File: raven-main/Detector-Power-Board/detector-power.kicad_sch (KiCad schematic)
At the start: 35 parts, among them J1 DeployLipo, J9 UCLipo, Q1 SQJQ100EL, T1 Transformer_1P_1S, U6 LM5185QPWPRQ1, U7 TPS7A4701xRGW, U8 TPS7A4701xRGW

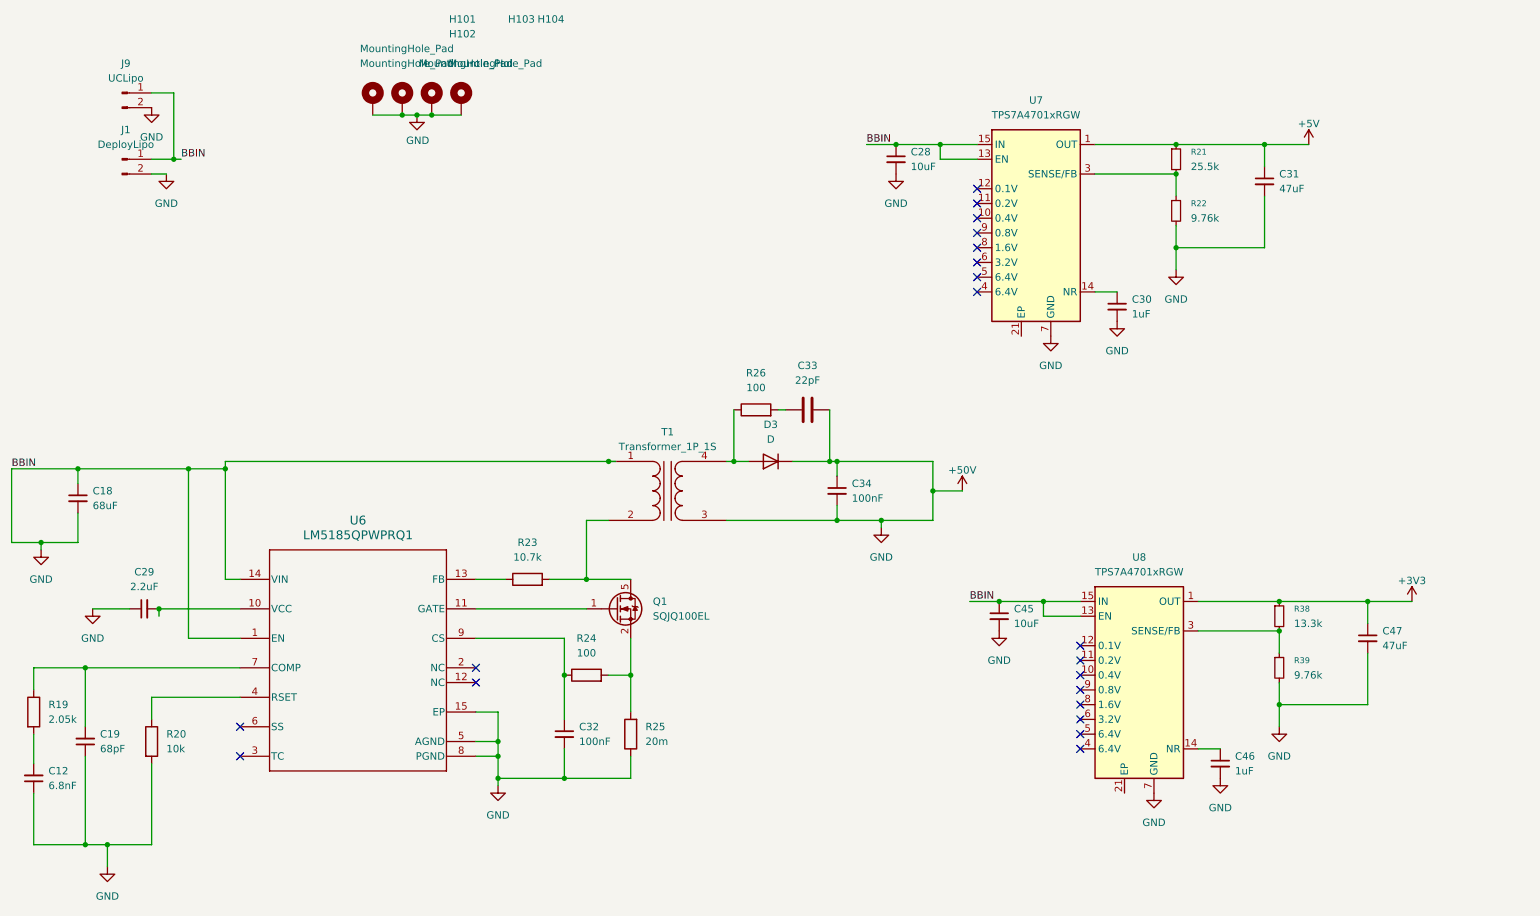
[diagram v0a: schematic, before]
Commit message: Added detector integration to power
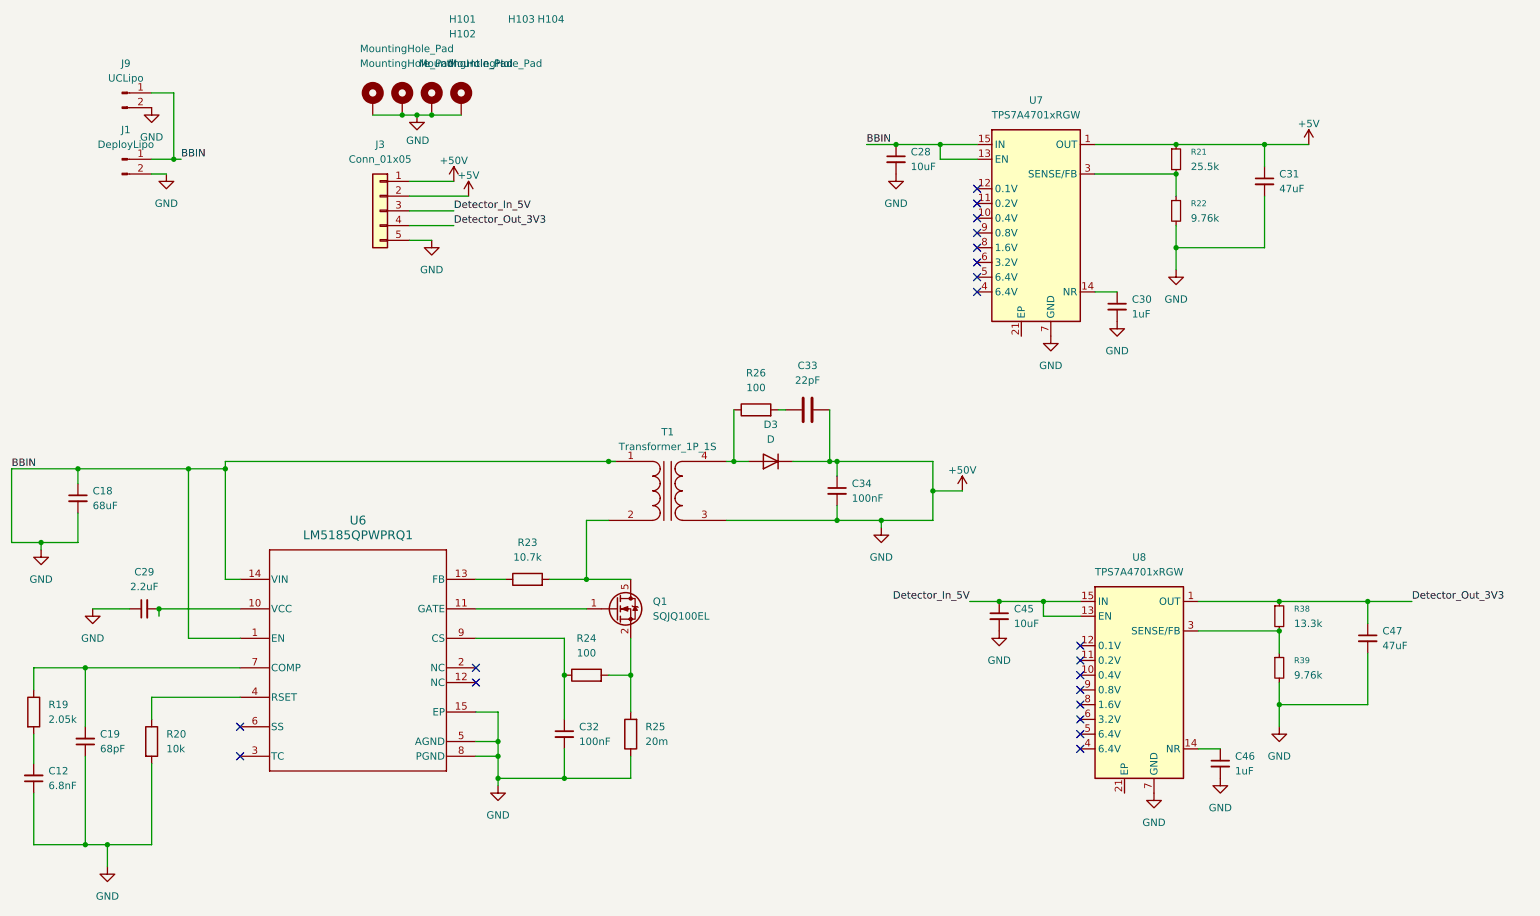
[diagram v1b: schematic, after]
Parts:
- added J3: Conn_01x05, symbol Connector_Generic:Conn_01x05
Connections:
- net +50V: now also J3.1 (Pin_1), J3.5 (Pin_5); no longer C45.1, U8.13 (EN), U8.15 (IN), U8.16 (IN)
- net +5V: now also J3.2 (Pin_2)
- net +3V3 renamed Detector_Out_3V3
- net Detector_Out_3V3: now also J3.4 (Pin_4)
- new net Detector_In_5V: C45.1, J3.3 (Pin_3), U8.13 (EN), U8.15 (IN), U8.16 (IN)

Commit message: Added on/off
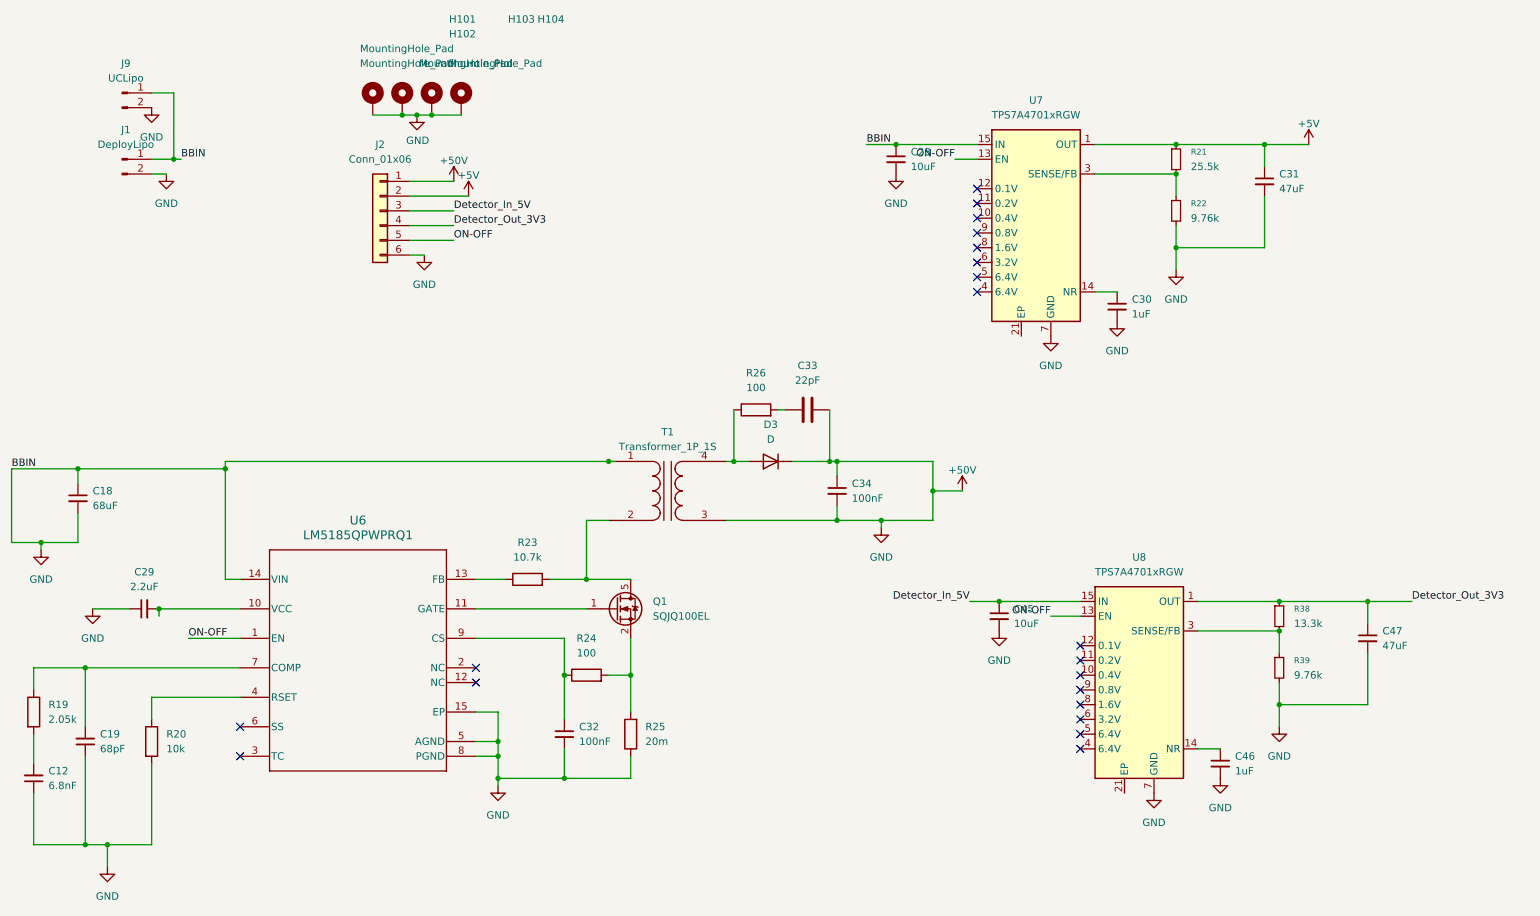
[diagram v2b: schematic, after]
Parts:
- removed J3: Conn_01x05, symbol Connector_Generic:Conn_01x05
- added J2: Conn_01x06, symbol Connector_Generic:Conn_01x06
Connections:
- net +50V: now also J2.1 (Pin_1), J2.6 (Pin_6); no longer U6.1 (EN), U7.13 (EN)
- net +5V: now also J2.2 (Pin_2)
- net Detector_In_5V: now also J2.3 (Pin_3); no longer U8.13 (EN)
- net Detector_Out_3V3: now also J2.4 (Pin_4)
- new net ON-OFF: J2.5 (Pin_5), U6.1 (EN), U7.13 (EN), U8.13 (EN)

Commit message: Organising parts in layout
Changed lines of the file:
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@@
-	)
-	(junction
-		(at 63.5 120.65)
-		(diameter 0)
-		(color 0 0 0 0)
 	)
 	(junction
@@
 		)
 		(stroke
-			(width 0)
-			(type default)
-		)
-	)
-	(wire
-		(pts
-			(xy 63.5 120.65) (xy 63.5 121.92)
-		)
-		(stroke

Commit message: Relabelled power board
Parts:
- J2: footprint (none) -> TerminalBlock_4Ucon:TerminalBlock_4Ucon_1x06_P3.50mm_Horizontal
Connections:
- net +50V renamed GND
- net +5V renamed Power_Out_5V
- net Detector_In_5V renamed Data_In_5V
- net Detector_Out_3V3 renamed Data_Out_3V3

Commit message: Corrected boost
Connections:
- net GND: no longer C18.1, C28.1, C33.2, C34.1, D3.1 (K), J1.1 (Pin_1), J2.1 (Pin_1), J9.1 (Pin_1), T1.1 (AA), U6.14 (VIN), U7.15 (IN), U7.16 (IN)
- new net BBIN: C18.1, C28.1, J1.1 (Pin_1), J9.1 (Pin_1), T1.1 (AA), U6.14 (VIN), U7.15 (IN), U7.16 (IN)
- new net Power_Out_50V: C33.2, C34.1, D3.1 (K), J2.1 (Pin_1)
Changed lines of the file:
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@@
-	)
-	(junction
-		(at 196.85 100.33)
-		(diameter 0)
-		(color 0 0 0 0)
 	)
 	(junction
@@
 	)
 	(junction
-		(at 187.96 105.41)
-		(diameter 0)
-		(color 0 0 0 0)
-	)
-	(junction
-		(at 43.18 109.22)
-		(diameter 0)
-		(color 0 0 0 0)
-	)
-	(junction
 		(at 107.95 35.56)
 		(diameter 0)
@@
 	(wire
 		(pts
-			(xy 38.1 96.52) (xy 38.1 109.22)
-		)
-		(stroke
-			(width 0)
-			(type default)
-		)
-	)
-	(wire
-		(pts
 			(xy 100.33 35.56) (xy 107.95 35.56)
 		)
@@
 	(wire
 		(pts
-			(xy 187.96 105.41) (xy 196.85 105.41)
-		)
-		(stroke
-			(width 0)
-			(type default)
-		)
-	)
-	(wire
-		(pts
-			(xy 38.1 109.22) (xy 43.18 109.22)
-		)
-		(stroke
-			(width 0)
-			(type default)
-		)
-	)
-	(wire
-		(pts
 			(xy 41.91 142.24) (xy 41.91 147.32)
 		)
@@
 		)
 		(stroke
-			(width 0)
-			(type default)
-		)
-	)
-	(wire
-		(pts
-			(xy 196.85 105.41) (xy 196.85 100.33)
-		)
-		(stroke
